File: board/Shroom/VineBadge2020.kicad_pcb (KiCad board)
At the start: 2 copper layers, 95 x 95.7 mm, 73 parts, among them IC1 ATTINY20-X, J1 CONN-TAGCONNECT-TC2050, SW2 SW_Push

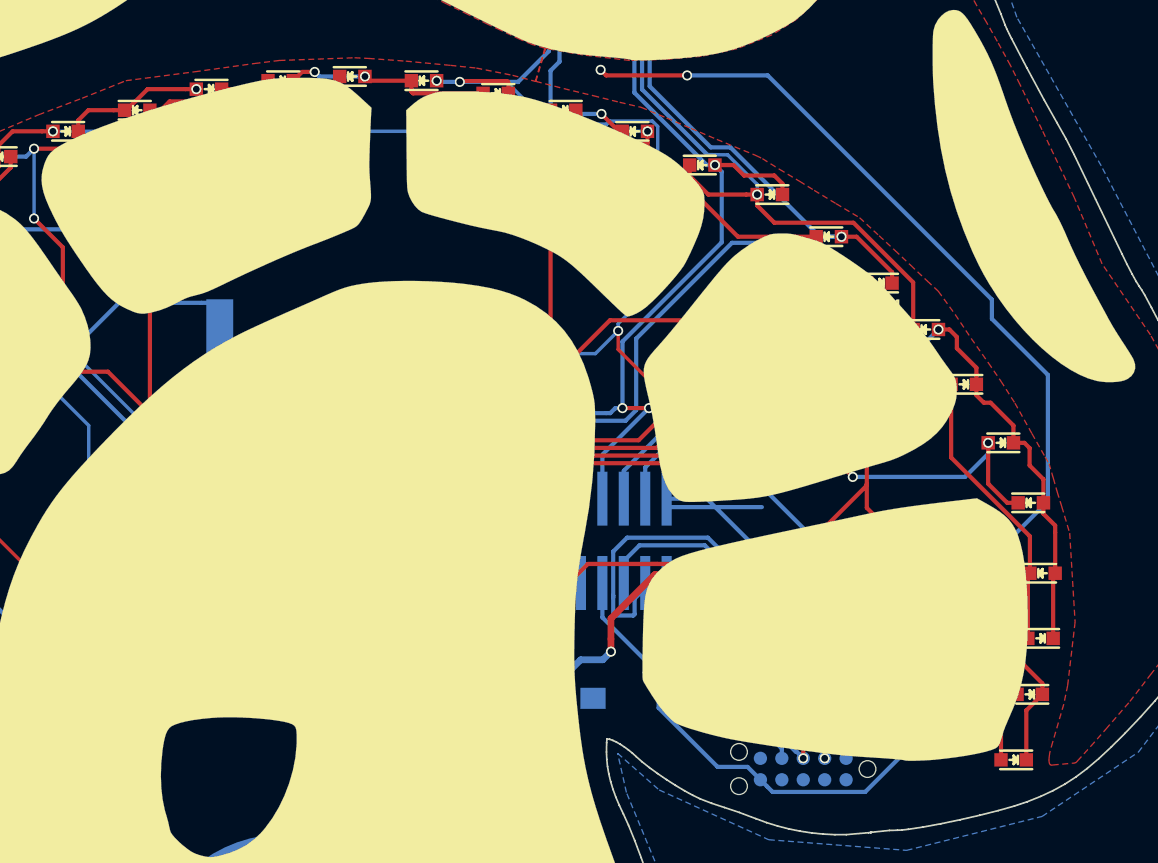
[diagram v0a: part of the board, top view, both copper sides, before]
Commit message: created a progmem led map, need ot test
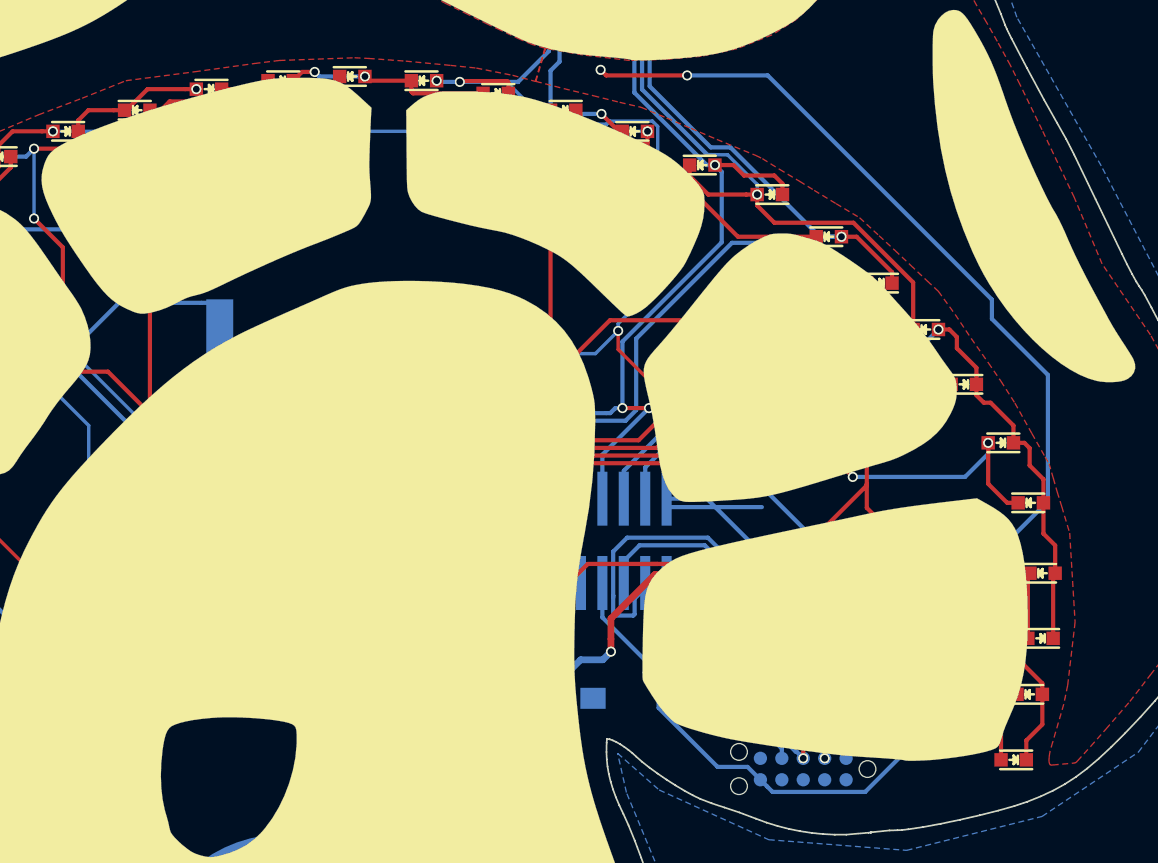
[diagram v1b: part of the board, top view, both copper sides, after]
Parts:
- turned D50 to 0 degrees
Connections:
- D50 pad 1: Net-(D14-Pad2) -> Net-(D10-Pad1)
- D50 pad 2: Net-(D10-Pad1) -> Net-(D14-Pad2)
- D51 pad 1: Net-(D13-Pad2) -> Net-(D14-Pad2)
- D52 pad 2: Net-(D13-Pad2) -> Net-(D14-Pad2)
- F1 pad 1: Net-(D53-Pad2) -> Net-(D57-Pad2)
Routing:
- net Net-(D13-Pad2): track 145.7 -> 128.7 mm
- net Net-(D14-Pad2): track 132.6 -> 138.3 mm

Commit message: removed programming stuff, getting ready for final revision. Just needs last checks
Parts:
- removed C1: 100nF, Capacitors_SMD:C_0805_HandSoldering
- removed C2: 1uF, Capacitors_SMD:C_0805_HandSoldering
- removed D53: D_Schottky, Diodes_SMD:SOD-323_HandSoldering
- removed J1: CONN-TAGCONNECT-TC2050, VineBadge2020:TC2050-All_Holes
- removed ON/OFF: SW_SPDT, VineBadge2020:JS202011JAQN-Handsolder
- removed R10: 1K, Resistors_SMD:R_0805_HandSoldering
- added D57: D_Schottky, Diodes_SMD:SOD-323_HandSoldering, B.Cu at (150.9, 123.7)
- F1: footprint Fuse_Holders_and_Fuses:Fuse_SMD1206_Reflow -> Resistors_SMD:R_0603_HandSoldering; moved to F.Cu
- SW2: footprint VineBadge2020:SW_SPST_EVQPE1_Handsolder -> Buttons_Switches_SMD:SW_SPST_TL3342
- moved G*** 44.3 mm to (122.2, 68.3)
- moved G*** 37.3 mm to (136.1, 64.0)
- moved F1 20.8 mm to (137.2, 140.0), turned to 180 degrees
- moved SW2 4.37 mm to (125.5, 86.9), turned to 0 degrees
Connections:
- BT1 pad 2: GND -> Net-(BT1-Pad2)
- F1 pad 1: Net-(D57-Pad2) -> GND
- F1 pad 2: Net-(F1-Pad2) -> Net-(BT1-Pad2)
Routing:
- net GND: track 169.5 -> 68.4 mm, vias 7 -> 3
- net Net-(BT1-Pad2): track 0.00 -> 55.9 mm, vias 0 -> 1
- net +BATT: track 52.4 -> 30.8 mm
- net /TCK: track 36.9 -> 21.8 mm
- net /TDI: track 31.2 -> 21.1 mm, vias 2 -> 1
- net /RST: track 39.1 -> 32.5 mm
- net Net-(BT1-Pad1): track 47.7 -> 43.0 mm
- net Net-(F1-Pad2): track 4.67 -> 0.00 mm
- net /BTN: track 50.7 -> 48.1 mm
- net Net-(D53-Pad2): track 2.59 -> 0.00 mm
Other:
- board text added: "+"
- board text added: "1"
- board text added: "PUSH"
- board text added: "REMOVE BATTERY WHEN NOT IN USE"
- board text added: "gh"
- board text added: "hi chat"

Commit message: kfdjkd
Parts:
- added REF**: KiCAD Logo, Symbols:Symbol_KiCAD-Logo_CopperAndSilkScreenTop, B.Cu at (164.1, 65.6)
- added REF**: Symbol_CreativeCommons_CopperTop_Type2_Small, Symbols:Symbol_CreativeCommons_CopperTop_Type2_Small, B.Cu at (175.2, 80.9)
- added REF***: OSHW-Logo2_14.6x12mm_Copper, Symbols:OSHW-Logo2_14.6x12mm_Copper, B.Cu at (113.0, 96.9)
- F1: value Fuse -> Polyfuse
- moved F1 15.9 mm to (152.2, 135.0), turned to 225 degrees
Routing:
- net Net-(BT1-Pad1): track 43.0 -> 7.08 mm
- net Net-(BT1-Pad2): track 55.9 -> 76.2 mm
- net /BTN: track 48.1 -> 51.9 mm
- net Net-(D1-Pad2): track 151.3 -> 153.8 mm
- net GND: track 68.4 -> 66.7 mm
- net /RST: track 32.5 -> 33.5 mm
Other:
- board text added: "CC-Attribution ShareAlike 4.0 International"
- board text added: "DESIGNED WITH"
- board text added: "First Run: /30"
